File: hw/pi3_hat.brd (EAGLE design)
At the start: 56.5 x 65 mm, 106 parts, among them J1 XT30P, J2 XT30P, U1 AP64351SO8EP, U10 CAT24C32SOIC8, U11 STM32G474CEU6, U12 TCAN334GSOT23, U13 TCAN334GSOT23, U2 DMMT5401, U3 DMG2305UX, U4 STM32G474CEU6, U5 TCAN334GSOT23, U6 TCAN334GSOT23, U7 STM32G474CEU6, U8 BMI088LGA16, U9 TCAN334GSOT23

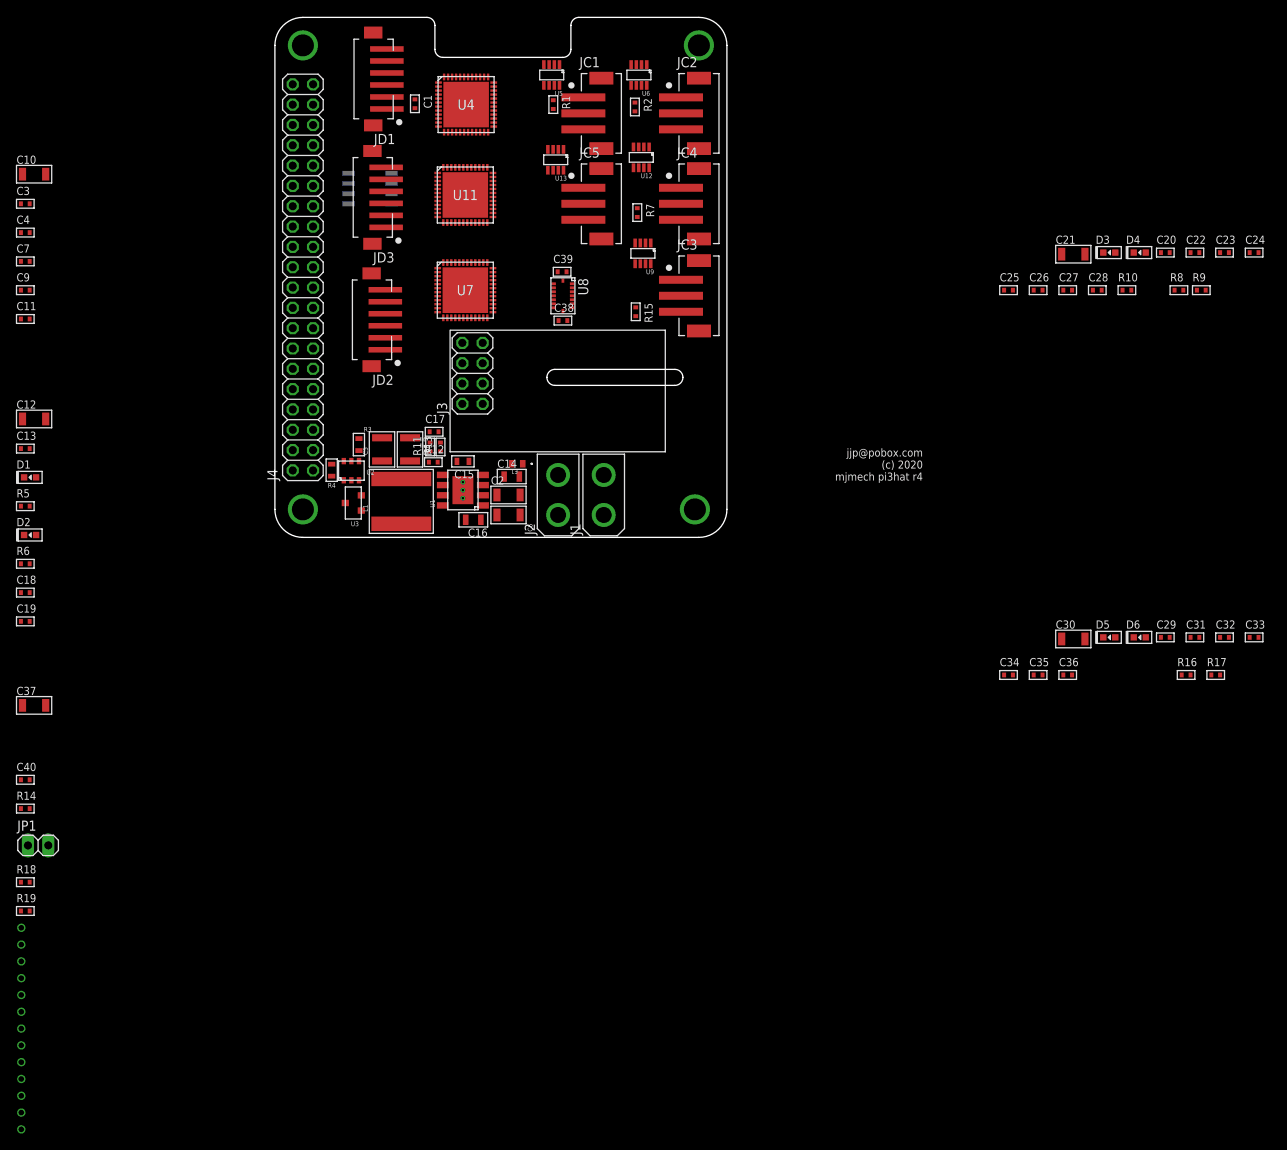
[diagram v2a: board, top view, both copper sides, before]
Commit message: Rough place all components
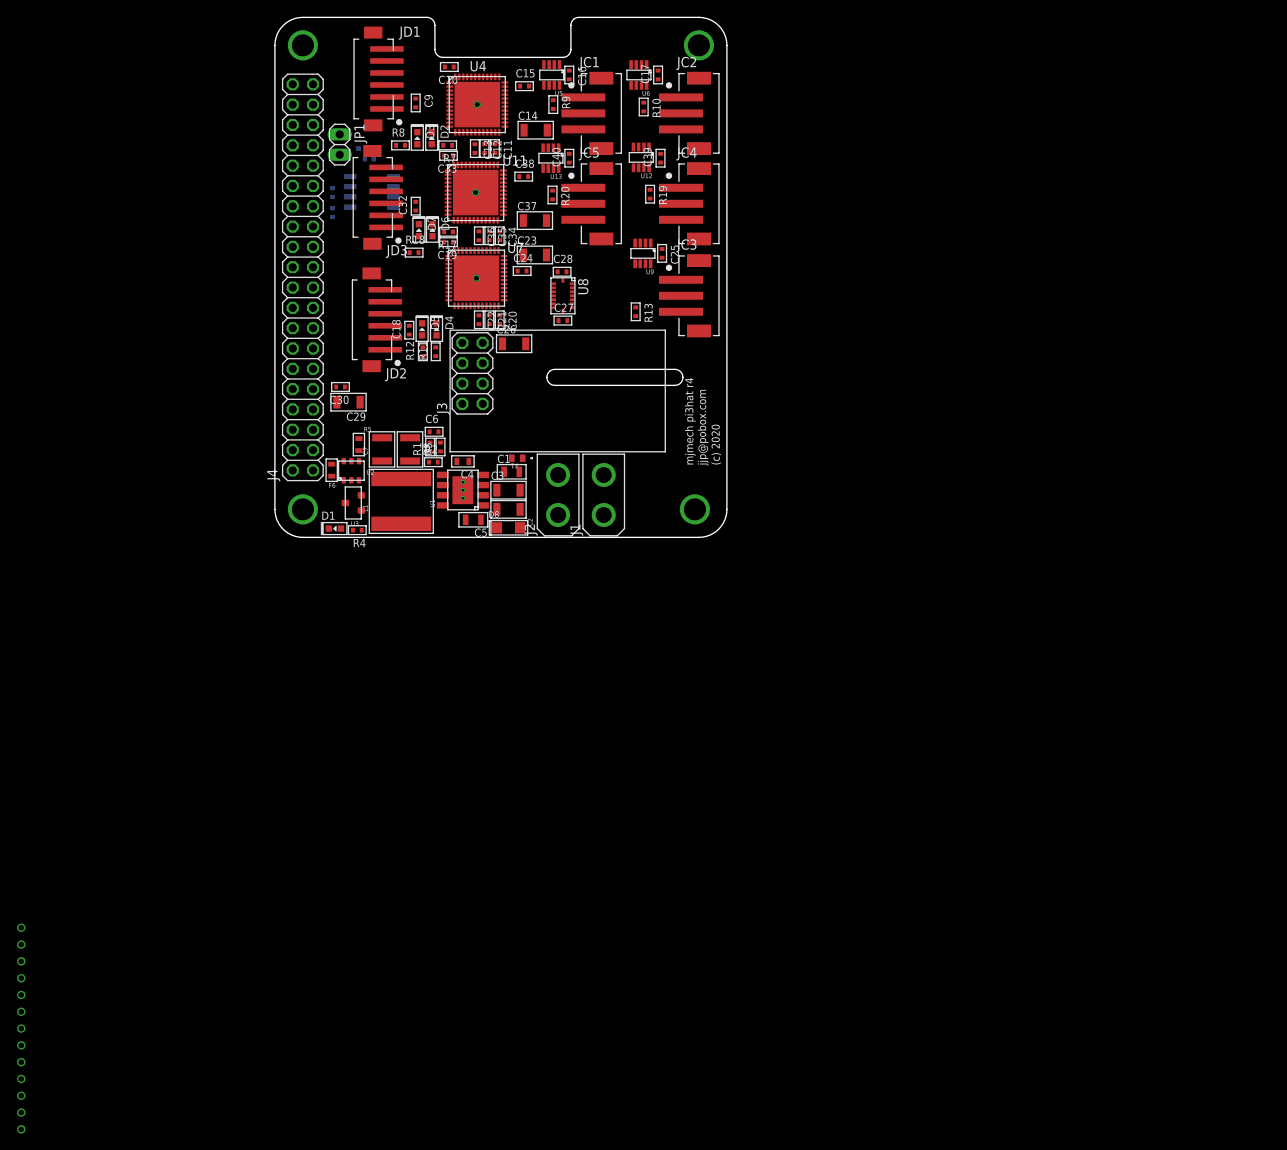
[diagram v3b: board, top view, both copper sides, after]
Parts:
- removed R6: (no value), mfpassives:R0402
- added D7: MF-LED-0603-RED, mfleds:LED0603
- added D8: 36V, pi3_hat:SMF
- added F6: 53.6k 1%, mfpassives:R0603
- added R20: 120, mfpassives:R0402
- C1: value 0.1uF -> .1uF 50V; device mfpassives:C0402 -> mfpassives:C0805
- C10, C12, C21, C30: value 10uF -> 0.1uF; device mfpassives:C1206 -> mfpassives:C0402
- C14: value .1uF 50V -> 10uF; device mfpassives:C0805 -> mfpassives:C1206
- C15: value 0.01uF -> 0.1uF; device mfpassives:C0603 -> mfpassives:C0402
- C16: value .1uF 50V -> 0.1uF; device mfpassives:C0805 -> mfpassives:C0402
- C17: value 3.3nF -> 0.1uF
- C20, C34: value 0.1uF -> 1uF
- C23, C29: value 0.1uF -> 10uF; device mfpassives:C0402 -> mfpassives:C1206
- C26: value 1uF -> 10uF; device mfpassives:C0402 -> mfpassives:C1206
- C3: value 0.1uF -> 10uF 50V; device mfpassives:C0402 -> mfpassives:C1206
- C35: value 1uF -> 0.1uF
- C4: value 0.1uF -> 0.01uF; device mfpassives:C0402 -> mfpassives:C0603
- C5: value 22uF 16V -> .1uF 50V; device mfpassives:C1210 -> mfpassives:C0805
- C6: value 10uF 50V -> 3.3nF; device mfpassives:C1206 -> mfpassives:C0402
- C7: value 0.1uF -> 22uF 16V; device mfpassives:C0402 -> mfpassives:C1210
- R1: value 120 -> 14k
- R10, R9: value (none) -> 120
- R11: value 14k -> 220
- R12: value 115k -> 220
- R13: value 22.1k -> 120
- R15: value 120 -> 3.9k 1%
- R16: value (none) -> 3.9k 1%
- R17: value (none) -> 220
- R18: value 3.9k 1% -> 220
- R19: value 3.9k 1% -> 120
- R2: value 120 -> 115k
- R3: value 10k 1% -> 22.1k; device mfpassives:R0603 -> mfpassives:R0402
- R4: value 53.6k 1% -> ~700; device mfpassives:R0603 -> mfpassives:R0402
- R5: value (none) -> 10k 1%; device mfpassives:R0402 -> mfpassives:R0603
- R7, R8: value 120 -> 220
- moved R16 122.6 mm to (7.20, 43.1), flipped to the bottom, turned to 270 degrees
- moved C31 119.3 mm to (11.8, 47.3), flipped to the bottom, turned to 180 degrees
- moved R19 118.9 mm to (46.9, 42.9), turned to 270 degrees
- moved C33 117.3 mm to (21.7, 47.7), turned to 180 degrees
- moved C32 114.6 mm to (17.6, 41.4), turned to 90 degrees
- moved R17 110.8 mm to (21.7, 38.2), turned to 180 degrees
- moved C29 106.2 mm to (9.20, 16.9), turned to 180 degrees
- moved C40 103.3 mm to (36.8, 47.4), turned to 90 degrees
- moved D6 102.0 mm to (19.7, 38.4), turned to 270 degrees
- moved R8 99.0 mm to (15.7, 49.0)
- moved C30 96.9 mm to (8.20, 18.8), turned to 180 degrees
- moved JP1 95.4 mm to (8.10, 49.1), turned to 270 degrees
- moved D5 94.1 mm to (18.4, 26.0), turned to 270 degrees
- moved R14 92.7 mm to (11.0, 48.6), flipped to the bottom
- moved R18 92.5 mm to (17.4, 35.6)
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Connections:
- removed net N$37 (its old number): D4.ANODE, R10.P$2
- new net N$52: D4.ANODE, R11.P$2
- new net N$9: D1.ANODE, R4.P$2
- net +3V3: now also C14.P$1, C15.P$1, C16.P$1, C17.P$1, C20.P$1, C29.P$1, R11.P$1, R12.P$1, R15.P$1, R7.P$1, R8.P$1, U11.1, U7.1; no longer C18.P$1, C3.P$1, C32.P$1, C4.P$1, C7.P$1, C9.P$1, R10.P$1, R19.P$1, R5.P$1, R6.P$1, R9.P$1
- net +5V: now also R4.P$1
- net GND: now also C16.P$2, D1.CATHODE, D8.A, F6.P$2, R5.P$2; no longer C5.P$2, R13.P$2, R4.P$2
- net ID_SCL: now also R16.P$2; no longer R19.P$2
- net ID_SDA: now also R15.P$2; no longer R18.P$2
- net N$1: now also R5.P$1; no longer R3.P$1
- net N$10: now also C1.P$1, C3.P$1, D8.C; no longer C14.P$1, C6.P$1
- net N$13: now also C9.P$1; no longer C1.P$1
- net N$14: now also C5.P$1; no longer C16.P$1
- net N$19: now also C4.P$1; no longer C15.P$1
- net N$2: now also R9.P$1; no longer R1.P$1
- net N$20: now also C5.P$2; no longer C16.P$2
- net N$21: now also C6.P$1, R1.P$2; no longer C17.P$1, R11.P$2
- net N$22: now also R1.P$1; no longer R11.P$1
- net N$23: now also R19.P$1; no longer R7.P$1
- net N$24: now also R2.P$2, R3.P$1; no longer R12.P$2, R13.P$1
- net N$25: now also R19.P$2; no longer R7.P$2
- net N$26: now also R20.P$1; no longer R8.P$1
- net N$27: now also R20.P$2; no longer R8.P$2
- net N$28: now also D3.ANODE, R8.P$2; no longer D1.ANODE, R5.P$2
- net N$29: now also D3.CATHODE; no longer D1.CATHODE
- net N$30: now also R7.P$2; no longer R6.P$2
- net N$32: now also C32.P$1; no longer C20.P$1
- net N$35: now also D7.ANODE, R18.P$2; no longer D3.ANODE, R9.P$2
- net N$36: now also D7.CATHODE; no longer D3.CATHODE
- net N$38: now also D6.CATHODE; no longer D4.CATHODE
- net N$4: now also R9.P$2; no longer R1.P$2
- net N$45: now also R13.P$1; no longer R15.P$1
- net N$46: now also R13.P$2; no longer R15.P$2
- net N$47: now also C18.P$1; no longer C29.P$1
- net N$5: now also F6.P$1; no longer R4.P$1
- net N$50: now also R12.P$2; no longer R16.P$2
- net N$53: now also D4.CATHODE; no longer D6.CATHODE
- net N$7: now also R10.P$1; no longer R2.P$1
- net N$8: now also R10.P$2; no longer R2.P$2
- net REGOUT: now also C7.P$1, R2.P$1; no longer C5.P$1, R12.P$1

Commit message: Rough silks
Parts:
- moved +5V 87.0 mm to (-5.50, 30.0)
- moved GND 87.0 mm to (-5.50, 27.9)
- moved REGOUT 87.0 mm to (-5.50, 34.2)
- moved SPI0_CS0 87.0 mm to (-5.50, 15.3)
- moved SPI0_MISO 87.0 mm to (-5.50, 11.1)
- moved SPI0_MOSI 87.0 mm to (-5.50, 9.00)
- moved SPI0_SCLK 87.0 mm to (-5.50, 13.2)
- moved SPI1_CS0 87.0 mm to (-5.50, 25.8)
- moved SPI1_CS1 87.0 mm to (-5.50, 23.7)
- moved SPI1_MISO 87.0 mm to (-5.50, 19.5)
- moved SPI1_MOSI 87.0 mm to (-5.50, 17.4)
- moved SPI1_SCLK 87.0 mm to (-5.50, 21.6)
- moved V+ 87.0 mm to (-5.50, 32.1)
- moved JC5 17.1 mm to (53.3, 29.7)
- moved C14 12.4 mm to (32.2, 63.3)
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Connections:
- net N$23: now also JC3.1; no longer JC4.1
- net N$25: now also JC3.2; no longer JC4.2
- net N$26: now also JC4.1; no longer JC5.1
- net N$27: now also JC4.2; no longer JC5.2
- net N$45: now also JC5.1; no longer JC3.1
- net N$46: now also JC5.2; no longer JC3.2
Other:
- outline, holes or cut-outs redrawn
- board text added: "mjbots quad pi3hat r4"
- board text removed: "mjmech pi3hat r4"

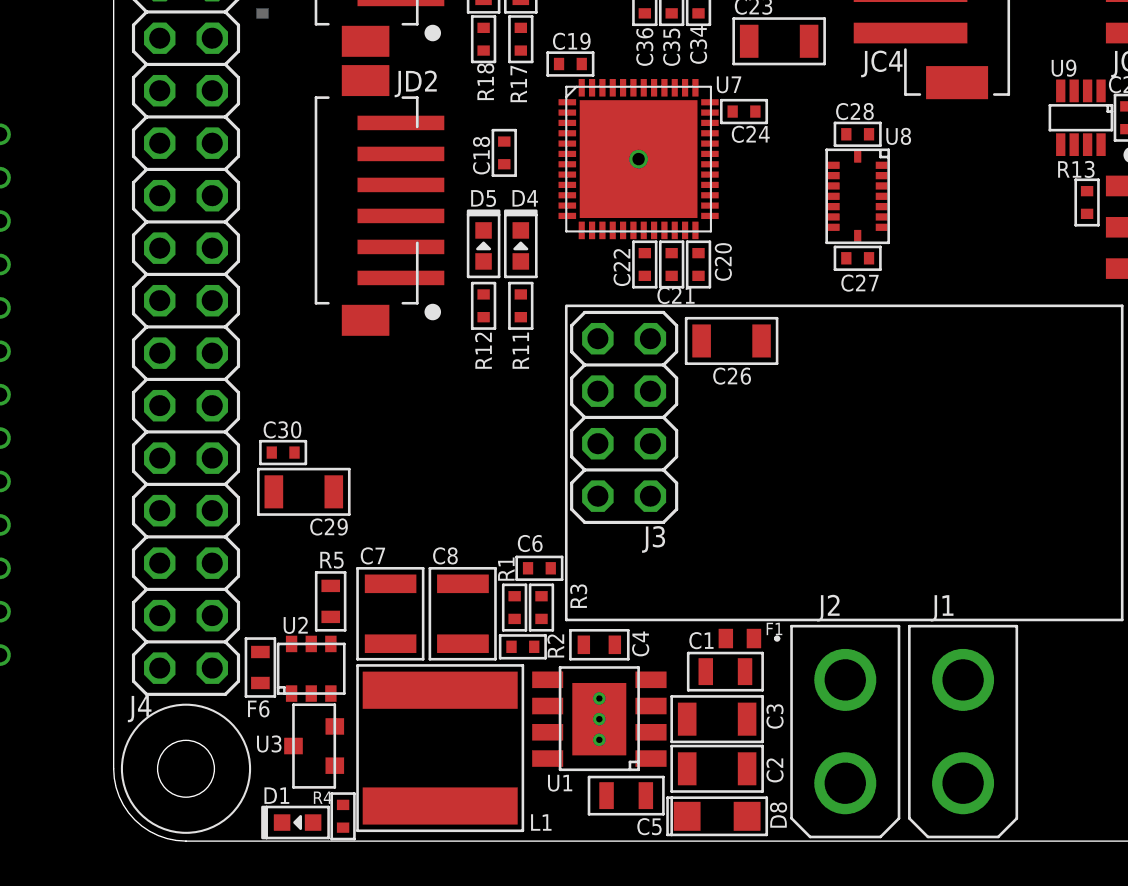
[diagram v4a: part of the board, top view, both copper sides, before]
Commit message: Route power input
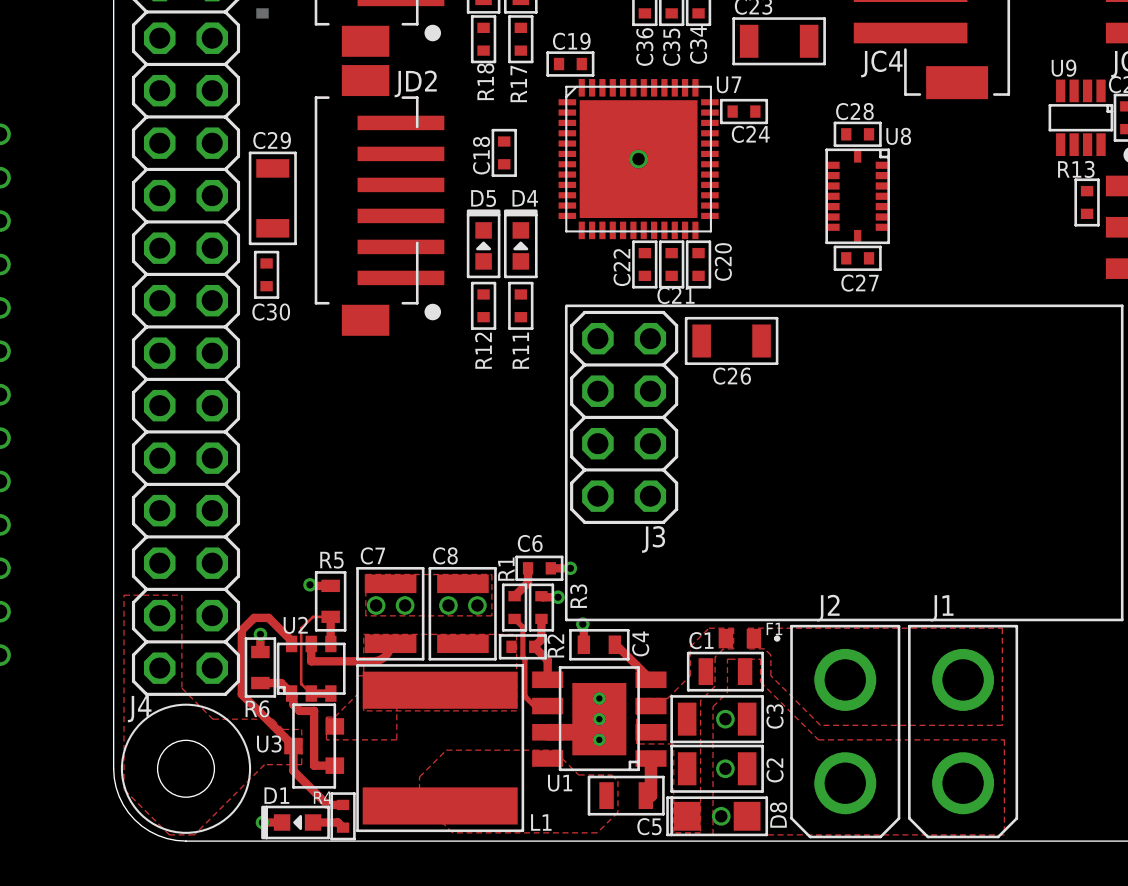
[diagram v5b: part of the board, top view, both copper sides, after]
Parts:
- moved C29 14.3 mm to (7.70, 31.1), turned to 90 degrees
- moved C30 8.64 mm to (7.40, 27.4), turned to 270 degrees
- renumbered F6 to R6
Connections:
- net N$10 renamed V+FUSED
- net N$20 renamed 5VSW
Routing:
- net +5V: track 0.00 -> 14.2 mm
- net GND: track 0.00 -> 8.48 mm, vias 3 -> 16
- net N$1: track 0.00 -> 7.28 mm
- net N$5: track 0.00 -> 7.07 mm
- net N$22: track 0.00 -> 5.25 mm
- net REGOUT: track 0.00 -> 5.03 mm
- net N$24: track 0.00 -> 3.36 mm
- net N$19: track 0.00 -> 2.45 mm
- net N$14: track 0.00 -> 2.04 mm
- net N$21: track 0.00 -> 1.62 mm
- net N$9: track 0.00 -> 1.55 mm
- added copper zone on layer 15, net +3V3
- added copper zone on layer 1, net +5V
- added copper zone on layer 1, net 5VSW
- added copper zone on layer 1, net GND
- added copper zone on layer 2, net GND
- added copper zone on layer 1, net REGOUT
- added copper zone on layer 1, net V+
- added copper zone on layer 1, net V+FUSED
